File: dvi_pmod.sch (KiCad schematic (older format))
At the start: 12 parts, among them J1 02x06, J2 Conn_01x02, J3 NOT_HDMI_A

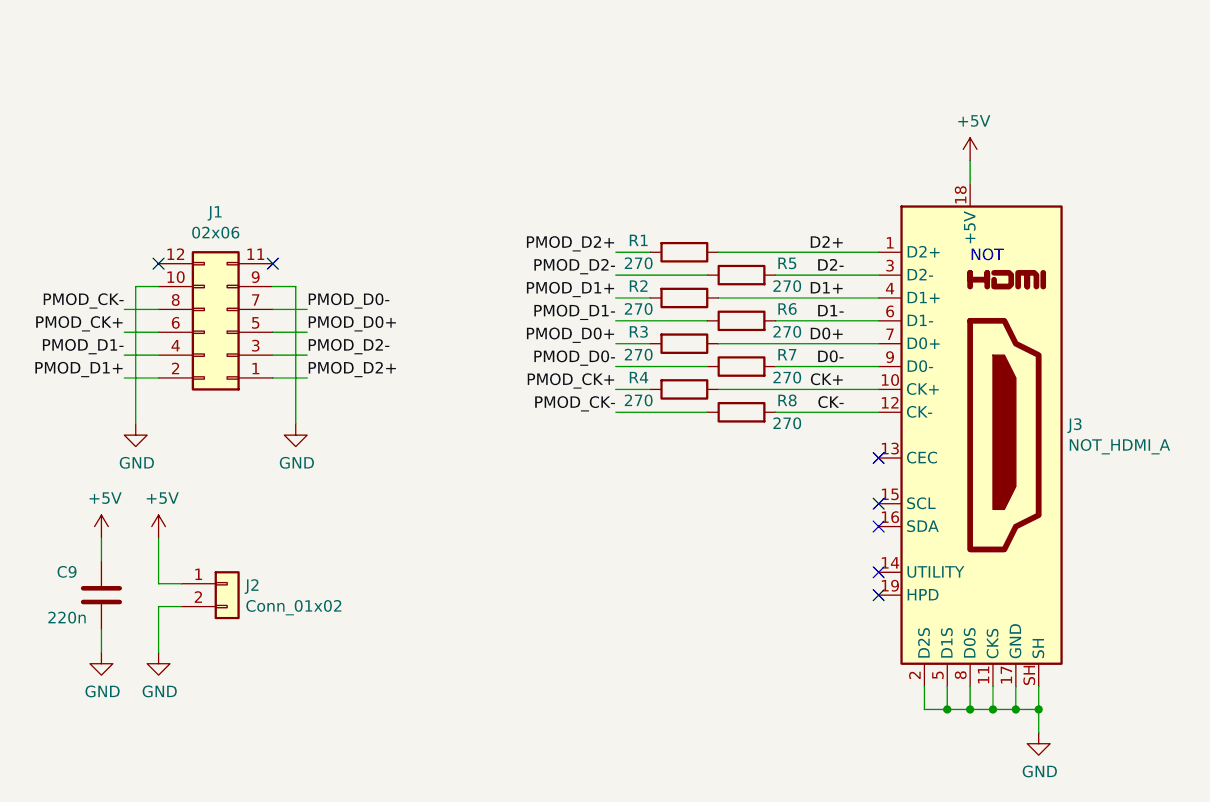
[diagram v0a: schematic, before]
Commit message: New pinout and new layout
Signed-off-by: Sylvain Munaut <tnt@246tNt.com>
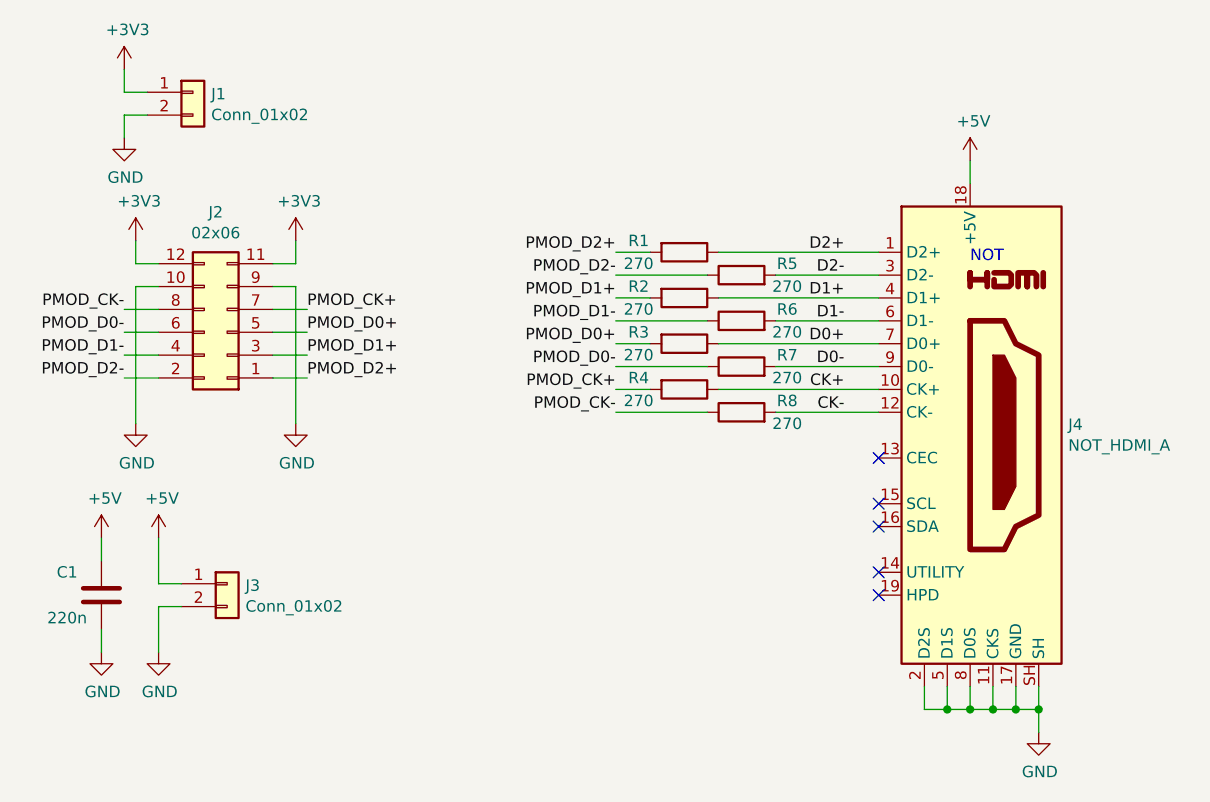
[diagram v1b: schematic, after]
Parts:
- added J1: Conn_01x02, Connector_PinHeader_2.54mm:PinHeader_1x02_P2.54mm_Vertical, symbol Connector_Generic:Conn_01x02
- renumbered C9 to C1, J1 to J2, J2 to J3, J3 to J4
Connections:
- net GND: now also J1.2 (Pin_2)
- net PMOD_CK+: now also J2.7 (Pin_7); no longer J2.6 (Pin_6)
- net PMOD_D0-: now also J2.6 (Pin_6); no longer J2.7 (Pin_7)
- net PMOD_D1+: now also J2.3 (Pin_3); no longer J2.2 (Pin_2)
- net PMOD_D2-: now also J2.2 (Pin_2); no longer J2.3 (Pin_3)
- net +3V3: now reaches J2.11 (Pin_11)
- net +3V3: now also J2.12 (Pin_12), J1.1 (Pin_1)
- no-connect marks 7 -> 5
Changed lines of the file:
@@
 EESchema Schematic File Version 4
-EELAYER 26 0
+EELAYER 30 0
 EELAYER END
 $Descr A4 11693 8268
@@
 $EndDescr
 $Comp
-L Connector:HDMI_A J3
+L Connector:HDMI_A J4
 U 1 1 5F61A1A0
 P 7750 3850
-F 0 "J3" H 8179 3896 50  0000 L CNN
+F 0 "J4" H 8179 3896 50  0000 L CNN
 F 1 "NOT_HDMI_A" H 8179 3805 50  0000 L CNN
 F 2 "dvi-pmod:HDMI-SS-53000" H 7775 3850 50  0001 C CNN
@@
 	1    0    0    -1
 $EndComp
-$Comp
-L Connector_Generic:Conn_02x06_Odd_Even J1
-U 1 1 5F61A52F
-P 4500 3400
-F 0 "J1" H 4550 2875 50  0000 C CNN
-F 1 "02x06" H 4550 2966 50  0000 C CNN
-F 2 "Connector_PinSocket_2.54mm:PinSocket_2x06_P2.54mm_Horizontal" H 4500 3400 50  0001 C CNN
-F 3 "~" H 4500 3400 50  0001 C CNN
-	1    4500 3400
-	-1   0    0    1
-$EndComp
 Wire Wire Line
 	4200 3200 4100 3200
@@
 	4100 3200 4100 3800
 $Comp
-L power:GND #PWR0103
+L power:GND #PWR06
 U 1 1 5F61A6C5
 P 4100 3800
-F 0 "#PWR0103" H 4100 3550 50  0001 C CNN
+F 0 "#PWR06" H 4100 3550 50  0001 C CNN
 F 1 "GND" H 4105 3627 50  0000 C CNN
 F 2 "" H 4100 3800 50  0001 C CNN
@@
 	4800 3200 4800 3800
 $Comp
-L power:GND #PWR0104
+L power:GND #PWR010
 U 1 1 5F61A75B
 P 4800 3800
-F 0 "#PWR0104" H 4800 3550 50  0001 C CNN
+F 0 "#PWR010" H 4800 3550 50  0001 C CNN
 F 1 "GND" H 4805 3627 50  0000 C CNN
 F 2 "" H 4800 3800 50  0001 C CNN
@@
 Connection ~ 8050 5050
 $Comp
-L power:GND #PWR0105
+L power:GND #PWR012
 U 1 1 5F6255C0
 P 8050 5150
-F 0 "#PWR0105" H 8050 4900 50  0001 C CNN
+F 0 "#PWR012" H 8050 4900 50  0001 C CNN
 F 1 "GND" H 8055 4977 50  0000 C CNN
 F 2 "" H 8050 5150 50  0001 C CNN
@@
 	7750 2750 7750 2650
 $Comp
-L power:+5V #PWR0106
+L power:+5V #PWR011
 U 1 1 5F625E53
 P 7750 2650
-F 0 "#PWR0106" H 7750 2500 50  0001 C CNN
+F 0 "#PWR011" H 7750 2500 50  0001 C CNN
 F 1 "+5V" H 7765 2823 50  0000 C CNN
 F 2 "" H 7750 2650 50  0001 C CNN
@@
 $EndComp
 $Comp
-L Connector_Generic:Conn_01x02 J2
+L Connector_Generic:Conn_01x02 J3
 U 1 1 5F626B92
 P 4500 4500
-F 0 "J2" H 4580 4492 50  0000 L CNN
+F 0 "J3" H 4580 4492 50  0000 L CNN
 F 1 "Conn_01x02" H 4580 4401 50  0000 L CNN
 F 2 "Connector_PinHeader_2.54mm:PinHeader_1x02_P2.54mm_Vertical" H 4500 4500 50  0001 C CNN
@@
 $EndComp
 $Comp
-L power:+5V #PWR0107
+L power:+5V #PWR07
 U 1 1 5F626C45
 P 4200 4300
-F 0 "#PWR0107" H 4200 4150 50  0001 C CNN
+F 0 "#PWR07" H 4200 4150 50  0001 C CNN
 F 1 "+5V" H 4215 4473 50  0000 C CNN
 F 2 "" H 4200 4300 50  0001 C CNN
@@
 $EndComp
 $Comp
-L power:GND #PWR0108
+L power:GND #PWR08
 U 1 1 5F626CE8
 P 4200 4800
-F 0 "#PWR0108" H 4200 4550 50  0001 C CNN
+F 0 "#PWR08" H 4200 4550 50  0001 C CNN
 F 1 "GND" H 4205 4627 50  0000 C CNN
 F 2 "" H 4200 4800 50  0001 C CNN
@@
 Wire Wire Line
 	4300 4600 4200 4600
-Text Label 4050 3400 2    50   ~ 0
+Text Label 4850 3300 0    50   ~ 0
 PMOD_CK+
 Text Label 4050 3300 2    50   ~ 0
@@
 Text Label 4850 3600 0    50   ~ 0
 PMOD_D2+
-Text Label 4850 3500 0    50   ~ 0
+Text Label 4050 3600 2    50   ~ 0
 PMOD_D2-
 Text Label 4850 3400 0    50   ~ 0
 PMOD_D0+
-Text Label 4850 3300 0    50   ~ 0
+Text Label 4050 3400 2    50   ~ 0
 PMOD_D0-
-Text Label 4050 3600 2    50   ~ 0
+Text Label 4850 3500 0    50   ~ 0
 PMOD_D1+
 Text Label 4050 3500 2    50   ~ 0
 PMOD_D1-
 $Comp
-L Device:C C9
+L Device:C C1
 U 1 1 5F630168
 P 3950 4550
-F 0 "C9" H 4100 4450 50  0000 C CNN
+F 0 "C1" H 4100 4450 50  0000 C CNN
 F 1 "220n" H 4100 4650 50  0000 C CNN
 F 2 "Capacitor_SMD:C_0402_1005Metric" H 3988 4400 50  0001 C CNN
@@
 Wire Wire Line
 	4200 4600 4200 4800
-NoConn ~ 4700 3100
-NoConn ~ 4200 3100
 $Comp
 L Device:R R1
@@
 Text Notes 7750 3100 0    50   ~ 0
 NOT
+$Comp
+L Connector_Generic:Conn_01x02 J1
+U 1 1 5FA32B49
+P 4350 2350
+F 0 "J1" H 4430 2342 50  0000 L CNN
+F 1 "Conn_01x02" H 4430 2251 50  0000 L CNN
+F 2 "Connector_PinHeader_2.54mm:PinHeader_1x02_P2.54mm_Vertical" H 4350 2350 50  0001 C CNN
+F 3 "~" H 4350 2350 50  0001 C CNN
+	1    4350 2350
+	1    0    0    -1
+$EndComp
+$Comp
+L power:GND #PWR04
+U 1 1 5FA33BF3
+P 4050 2550
+F 0 "#PWR04" H 4050 2300 50  0001 C CNN
+F 1 "GND" H 4055 2377 50  0000 C CNN
+F 2 "" H 4050 2550 50  0001 C CNN
+F 3 "" H 4050 2550 50  0001 C CNN
+	1    4050 2550
+	1    0    0    -1
+$EndComp
+Wire Wire Line
+	4150 2450 4050 2450
+Wire Wire Line
+	4050 2450 4050 2550
+$Comp
+L power:+3V3 #PWR09
+U 1 1 5FA34F14
+P 4800 3000
+F 0 "#PWR09" H 4800 2850 50  0001 C CNN
+F 1 "+3V3" H 4815 3173 50  0000 C CNN
+F 2 "" H 4800 3000 50  0001 C CNN
+F 3 "" H 4800 3000 50  0001 C CNN
+	1    4800 3000
+	1    0    0    -1
+$EndComp
+$Comp
+L Connector_Generic:Conn_02x06_Odd_Even J2
+U 1 1 5F61A52F
+P 4500 3400
+F 0 "J2" H 4550 2875 50  0000 C CNN
+F 1 "02x06" H 4550 2966 50  0000 C CNN
+F 2 "Connector_PinSocket_2.54mm:PinSocket_2x06_P2.54mm_Horizontal" H 4500 3400 50  0001 C CNN
+F 3 "~" H 4500 3400 50  0001 C CNN
+	1    4500 3400
+	-1   0    0    1
+$EndComp
+$Comp
+L power:+3V3 #PWR05
+U 1 1 5FA35886
+P 4100 3000
+F 0 "#PWR05" H 4100 2850 50  0001 C CNN
+F 1 "+3V3" H 4115 3173 50  0000 C CNN
+F 2 "" H 4100 3000 50  0001 C CNN
+F 3 "" H 4100 3000 50  0001 C CNN
+	1    4100 3000
+	1    0    0    -1
+$EndComp
+Wire Wire Line
+	4100 3000 4100 3100
+Wire Wire Line
+	4100 3100 4200 3100
+Wire Wire Line
+	4700 3100 4800 3100
+Wire Wire Line
+	4800 3100 4800 3000
+$Comp
+L power:+3V3 #PWR03
+U 1 1 5FA378D1
+P 4050 2250
+F 0 "#PWR03" H 4050 2100 50  0001 C CNN
+F 1 "+3V3" H 4065 2423 50  0000 C CNN
+F 2 "" H 4050 2250 50  0001 C CNN
+F 3 "" H 4050 2250 50  0001 C CNN
+	1    4050 2250
+	1    0    0    -1
+$EndComp
+Wire Wire Line
+	4050 2250 4050 2350
+Wire Wire Line
+	4050 2350 4150 2350
 $EndSCHEMATC
